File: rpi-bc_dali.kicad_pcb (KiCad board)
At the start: 2 copper layers, 59 x 85 mm, 5 parts, among them J1 Raspberry_Pi_2_3, J2 Conn_01x04, J3 Conn_01x04, J4 Conn_01x04, J5 Conn_01x04

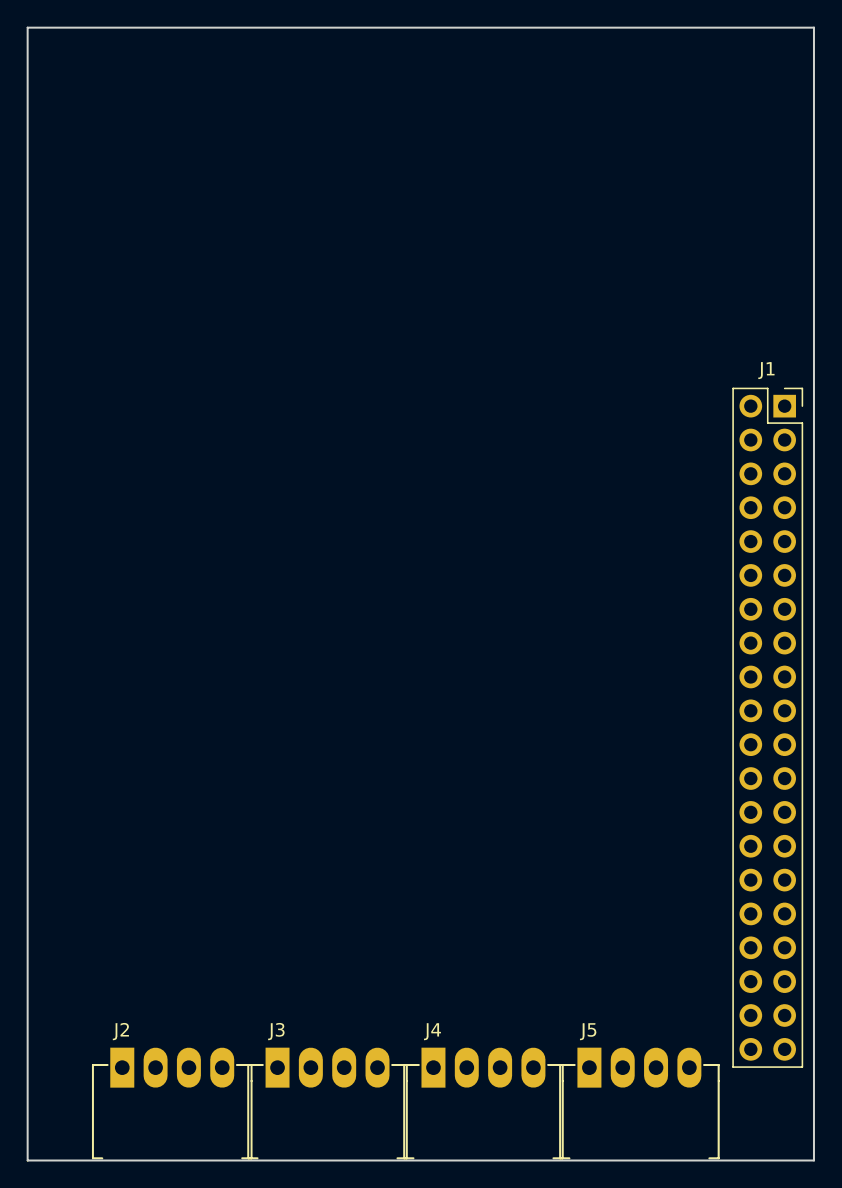
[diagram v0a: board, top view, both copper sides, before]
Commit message: master : first pass at layout
 - minor adjustments to schematic for trace flow
 - all nets routed and polygon's poured.
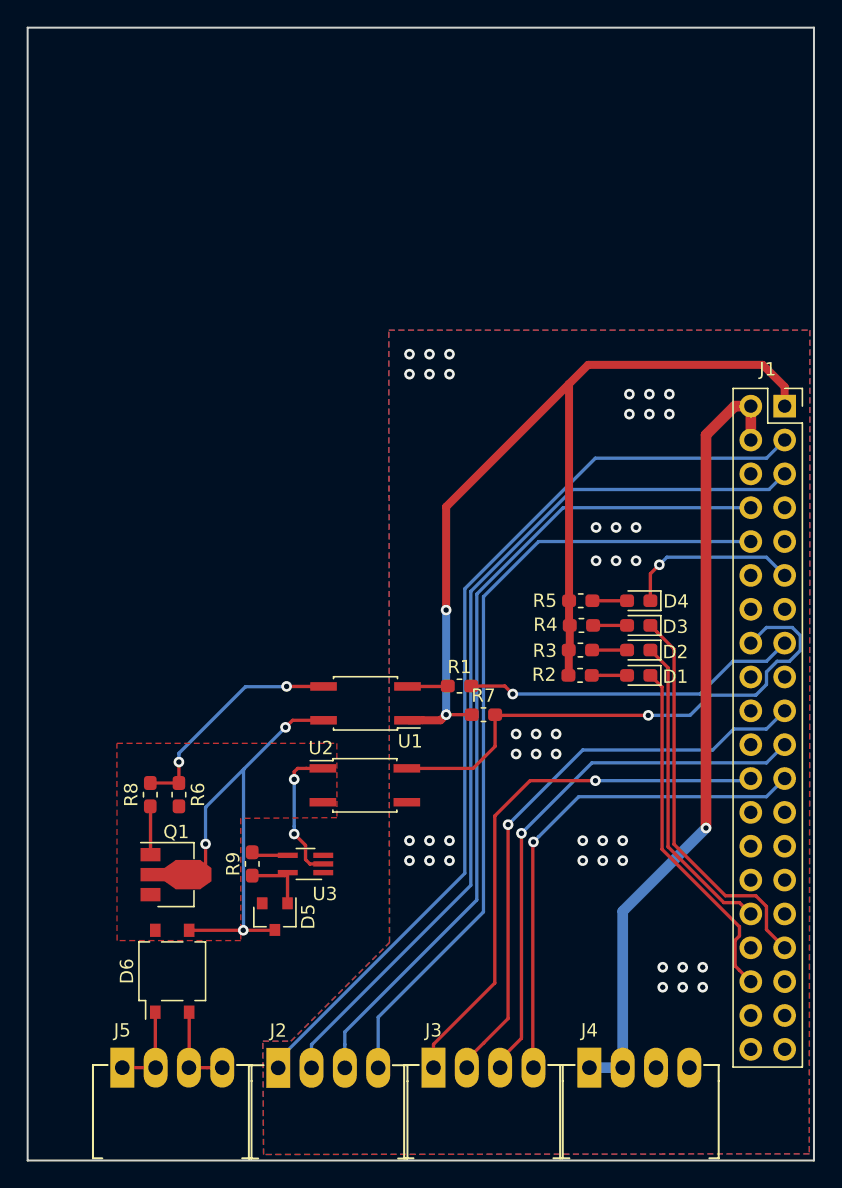
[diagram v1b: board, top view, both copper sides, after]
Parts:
- added D1: LED, LED_SMD:LED_0603_1608Metric_Pad1.05x0.95mm_HandSolder, F.Cu at (135.2, 103.6)
- added D2: LED, LED_SMD:LED_0603_1608Metric_Pad1.05x0.95mm_HandSolder, F.Cu at (135.2, 101.7)
- added D3: LED, LED_SMD:LED_0603_1608Metric_Pad1.05x0.95mm_HandSolder, F.Cu at (135.2, 99.8)
- added D4: LED, LED_SMD:LED_0603_1608Metric_Pad1.05x0.95mm_HandSolder, F.Cu at (135.2, 98.0)
- added D5: BZX84Cxx, Diode_SMD:D_SOT-23_ANK, F.Cu at (107.9, 121.7)
- added D6: MB2S, Package_TO_SOT_SMD:TO-269AA, F.Cu at (100.2, 125.8)
- added Q1: BCX56, Package_TO_SOT_SMD:SOT-89-3, F.Cu at (100.0, 118.5)
- added R1: 390R, Resistor_SMD:R_0603_1608Metric_Pad1.05x0.95mm_HandSolder, F.Cu at (121.8, 104.4)
- added R2: 1K, Resistor_SMD:R_0603_1608Metric_Pad1.05x0.95mm_HandSolder, F.Cu at (130.8, 103.6)
- added R3: 1K, Resistor_SMD:R_0603_1608Metric_Pad1.05x0.95mm_HandSolder, F.Cu at (130.8, 101.7)
- added R4: 1K, Resistor_SMD:R_0603_1608Metric_Pad1.05x0.95mm_HandSolder, F.Cu at (130.9, 99.8)
- added R5: 1K, Resistor_SMD:R_0603_1608Metric_Pad1.05x0.95mm_HandSolder, F.Cu at (130.8, 98.0)
- added R6: 1K, Resistor_SMD:R_0603_1608Metric_Pad1.05x0.95mm_HandSolder, F.Cu at (100.7, 112.5)
- added R7: 3K3, Resistor_SMD:R_0603_1608Metric_Pad1.05x0.95mm_HandSolder, F.Cu at (123.5, 106.5)
- added R8: 390R, Resistor_SMD:R_0603_1608Metric_Pad1.05x0.95mm_HandSolder, F.Cu at (98.5, 112.5)
- added R9: 560R, Resistor_SMD:R_0603_1608Metric_Pad1.05x0.95mm_HandSolder, F.Cu at (106.2, 117.8)
- added U1: HCPL-181, Package_SO:SO-4_4.4x3.6mm_P2.54mm, F.Cu at (114.7, 105.7)
- added U2: HCPL-181, Package_SO:SO-4_4.4x3.6mm_P2.54mm, F.Cu at (114.7, 111.8)
- added U3: PSSI2021SAY, Package_TO_SOT_SMD:SOT-353_SC-70-5_Handsoldering, F.Cu at (110.2, 117.8)
- moved J3 11.7 mm to (119.8, 133.0)
- moved J2 11.7 mm to (108.2, 133.1)
- renumbered J4 to J2, J5 to J4, J2 to J5
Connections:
- J1 pad 1: Net-(J1-Pad1) -> +3V3
- J1 pad 10: Net-(J1-Pad10) -> /UART_RXD
- J1 pad 11: Net-(J1-Pad11) -> /LED0
- J1 pad 14: Net-(J1-Pad14) -> GND
- J1 pad 15: Net-(J1-Pad15) -> /DALI_TX
- J1 pad 16: Net-(J1-Pad16) -> /DALI_RX
- J1 pad 17: Net-(J1-Pad17) -> +3V3
- J1 pad 19: Net-(J1-Pad19) -> /MOSI
- J1 pad 2: Net-(J1-Pad2) -> +5V
- J1 pad 20: Net-(J1-Pad20) -> GND
- J1 pad 21: Net-(J1-Pad21) -> /MISO
- J1 pad 23: Net-(J1-Pad23) -> /SCLK
- J1 pad 24: Net-(J1-Pad24) -> /CSN
- J1 pad 25: Net-(J1-Pad25) -> GND
- J1 pad 3: Net-(J1-Pad3) -> /I2C_SDA
- J1 pad 30: Net-(J1-Pad30) -> GND
- J1 pad 32: Net-(J1-Pad32) -> /LED2
- J1 pad 33: Net-(J1-Pad33) -> /LED1
- J1 pad 34: Net-(J1-Pad34) -> GND
- J1 pad 36: Net-(J1-Pad36) -> /LED3
- J1 pad 39: Net-(J1-Pad39) -> GND
- J1 pad 4: Net-(J1-Pad4) -> +5V
- J1 pad 5: Net-(J1-Pad5) -> /I2C_SCL
- J1 pad 6: Net-(J1-Pad6) -> GND
- J1 pad 8: Net-(J1-Pad8) -> /UART_TXD
- J1 pad 9: Net-(J1-Pad9) -> GND
- J2 pad 1: Net-(J4-Pad1) -> /I2C_SDA
- J2 pad 2: Net-(J4-Pad2) -> /I2C_SCL
- J2 pad 3: Net-(J4-Pad3) -> /UART_TXD
- J2 pad 4: Net-(J4-Pad4) -> /UART_RXD
- J3 pad 1: Net-(J3-Pad1) -> /CSN
- J3 pad 2: Net-(J3-Pad2) -> /MOSI
- J3 pad 3: Net-(J3-Pad3) -> /MISO
- J3 pad 4: Net-(J3-Pad4) -> /SCLK
- J4 pad 1: Net-(J5-Pad1) -> +5V
- J4 pad 2: Net-(J5-Pad2) -> +5V
- J4 pad 3: Net-(J5-Pad3) -> GND
- J4 pad 4: Net-(J5-Pad4) -> GND
- J5 pad 1: Net-(J2-Pad1) -> Net-(D6-Pad1)
- J5 pad 2: Net-(J2-Pad2) -> Net-(D6-Pad1)
- J5 pad 3: Net-(J2-Pad3) -> Net-(D6-Pad2)
- J5 pad 4: Net-(J2-Pad4) -> Net-(D6-Pad2)
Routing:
- net +3V3: track 0.00 -> 74.5 mm, vias 0 -> 2
- net /I2C_SDA: track 0.00 -> 70.4 mm
- net /I2C_SCL: track 0.00 -> 68.1 mm
- net /UART_TXD: track 0.00 -> 62.9 mm
- net /UART_RXD: track 0.00 -> 60.4 mm
- net +5V: track 0.00 -> 59.4 mm, vias 0 -> 1
- net /MOSI: track 0.00 -> 43.8 mm, vias 0 -> 1
- net /CSN: track 0.00 -> 41.7 mm, vias 0 -> 1
- net /MISO: track 0.00 -> 41.7 mm, vias 0 -> 1
- net /DALI_RX: track 0.00 -> 40.7 mm, vias 0 -> 1
- net Net-(D5-Pad1): track 0.00 -> 39.7 mm, vias 0 -> 3
- net /SCLK: track 0.00 -> 37.8 mm, vias 0 -> 1
- net /LED1: track 0.00 -> 29.7 mm
- net /LED3: track 0.00 -> 26.4 mm
- net /DALI_TX: track 0.00 -> 25.4 mm, vias 0 -> 1
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- added copper zone on F.Cu, net /GND_ISO
- added copper zone on B.Cu, net GND
- added copper zone on F.Cu, net GND

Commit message: master: updates to layout
 - fixed placement bug in GPIO connector.
 - re-routed all nets.
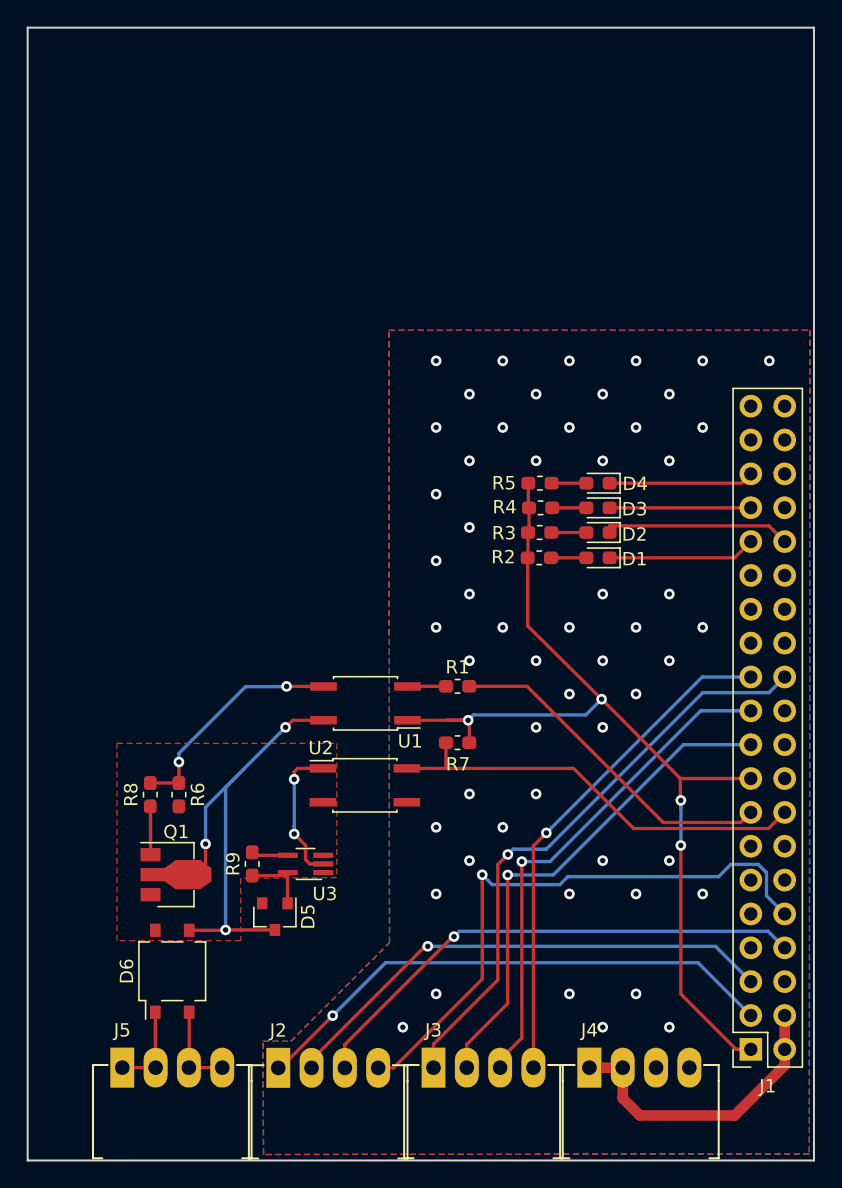
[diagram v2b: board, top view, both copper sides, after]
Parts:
- moved J1 48.3 mm to (143.6, 131.7), turned to 180 degrees
- moved D2 9.34 mm to (132.1, 92.9)
- moved R3 9.34 mm to (127.8, 92.9)
- moved R2 9.34 mm to (127.7, 94.8)
- moved D1 9.34 mm to (132.1, 94.8)
- moved D3 9.34 mm to (132.1, 91.0)
- moved D4 9.34 mm to (132.1, 89.2)
- moved R4 9.34 mm to (127.8, 91.0)
- moved R5 9.34 mm to (127.8, 89.2)
- moved R7 2.86 mm to (121.6, 108.7), turned to 180 degrees
- moved R1 0.14 mm to (121.6, 104.4)
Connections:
- J1 pad 11: /LED0 -> Net-(J1-Pad11)
- J1 pad 31: Net-(J1-Pad31) -> /LED3
- J1 pad 35: Net-(J1-Pad35) -> /LED0
- J1 pad 36: /LED3 -> Net-(J1-Pad36)
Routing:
- net +5V: track 59.4 -> 22.8 mm, vias 1 -> 0
- net /I2C_SDA: track 70.4 -> 40.4 mm, vias 0 -> 1
- net /I2C_SCL: track 68.1 -> 38.4 mm, vias 0 -> 1
- net /UART_TXD: track 62.9 -> 38.8 mm, vias 0 -> 1
- net /LED1: track 29.7 -> 10.6 mm
- net /UART_RXD: track 60.4 -> 44.6 mm, vias 0 -> 1
- net /LED3: track 26.4 -> 11.1 mm
- net /LED2: track 23.7 -> 14.2 mm
- net /DALI_RX: track 40.7 -> 32.7 mm, vias 1 -> 0
- net /MOSI: track 43.8 -> 38.0 mm
- net /CSN: track 41.7 -> 45.1 mm
- net /MISO: track 41.7 -> 39.0 mm
- net /LED0: track 13.2 -> 10.9 mm, vias 1 -> 0
- net +3V3: track 74.5 -> 74.1 mm, vias 2 -> 4
- net /DALI_TX: track 25.4 -> 25.7 mm, vias 1 -> 0
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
